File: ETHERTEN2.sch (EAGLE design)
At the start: 103 parts, among them IC1 MC33269DT-5.0, IC2 APX811-44UG-7, IC3 ATMEGA16U2-MU, IC4 LM358D, IC5 ATMEGA328P TQFP32, IC6 W5100SQFP80, IC7 MCP24AA025E48, J1 DC_2_1MM, P1 USB-6PSMT, P2 ICSP:MAIN, P3 ICSP:USB, P4 microSD, Q1 FDN340P, Q2 2N7002, Q3 2N7002, U1 HY931147C-RJ45, X1 16MHz, X2 25MHz, X3 16MHz

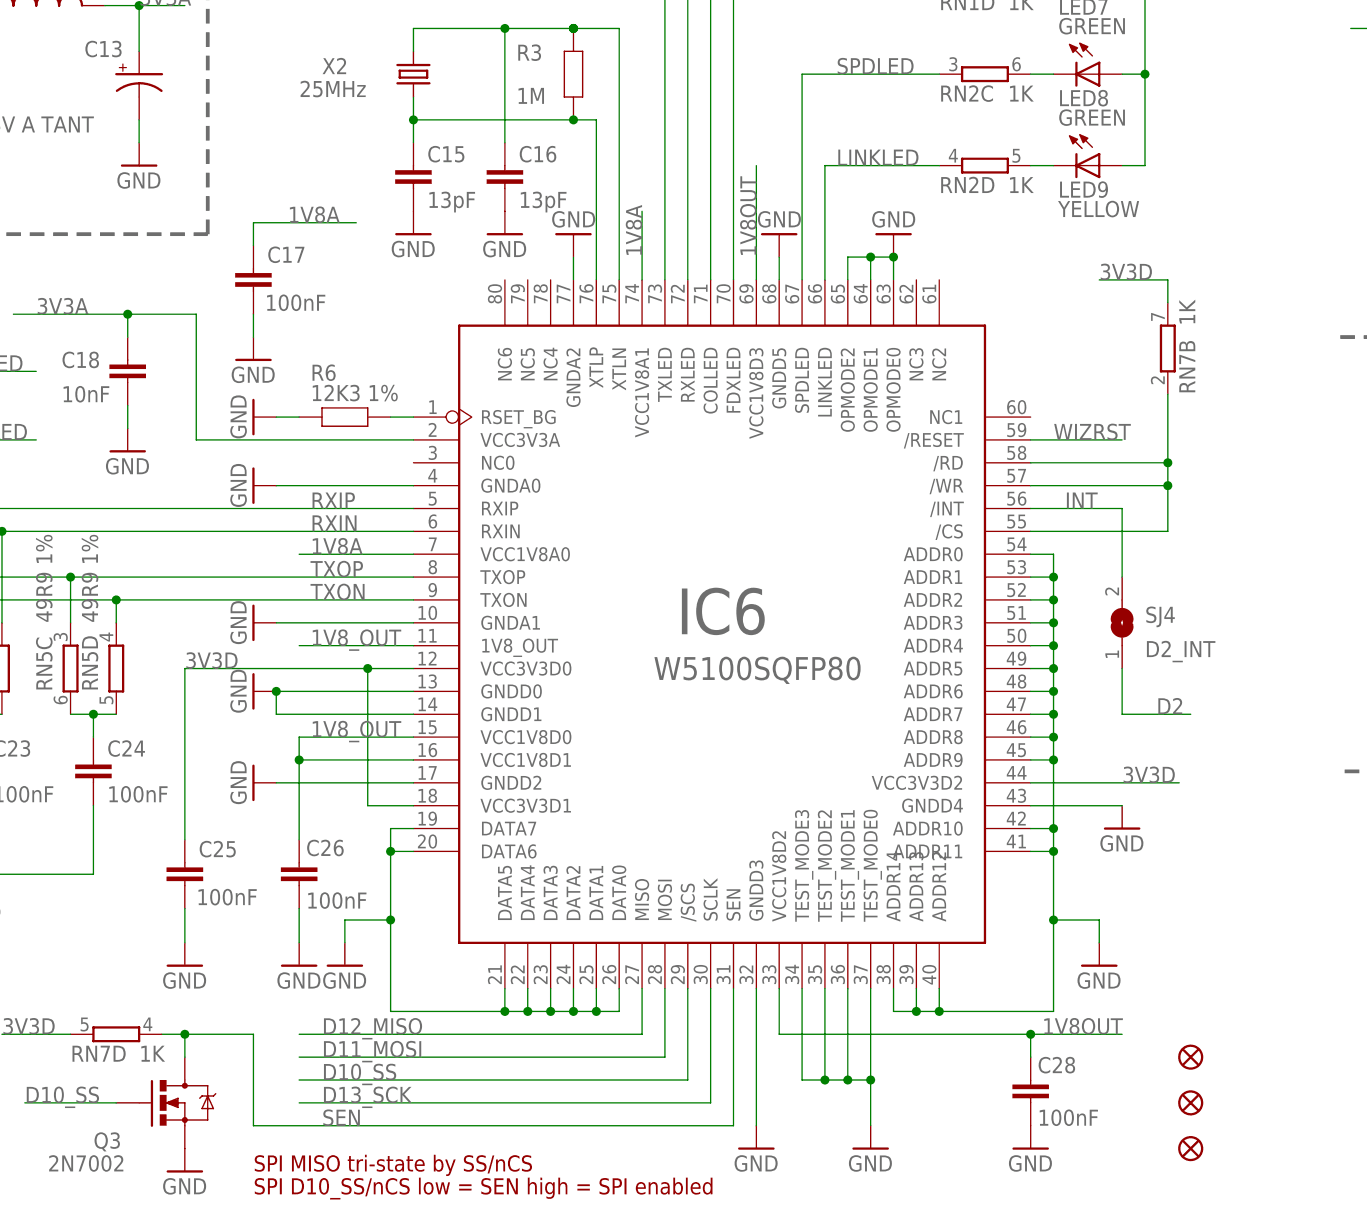
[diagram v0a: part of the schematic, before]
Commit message: Ethernet chip conversion
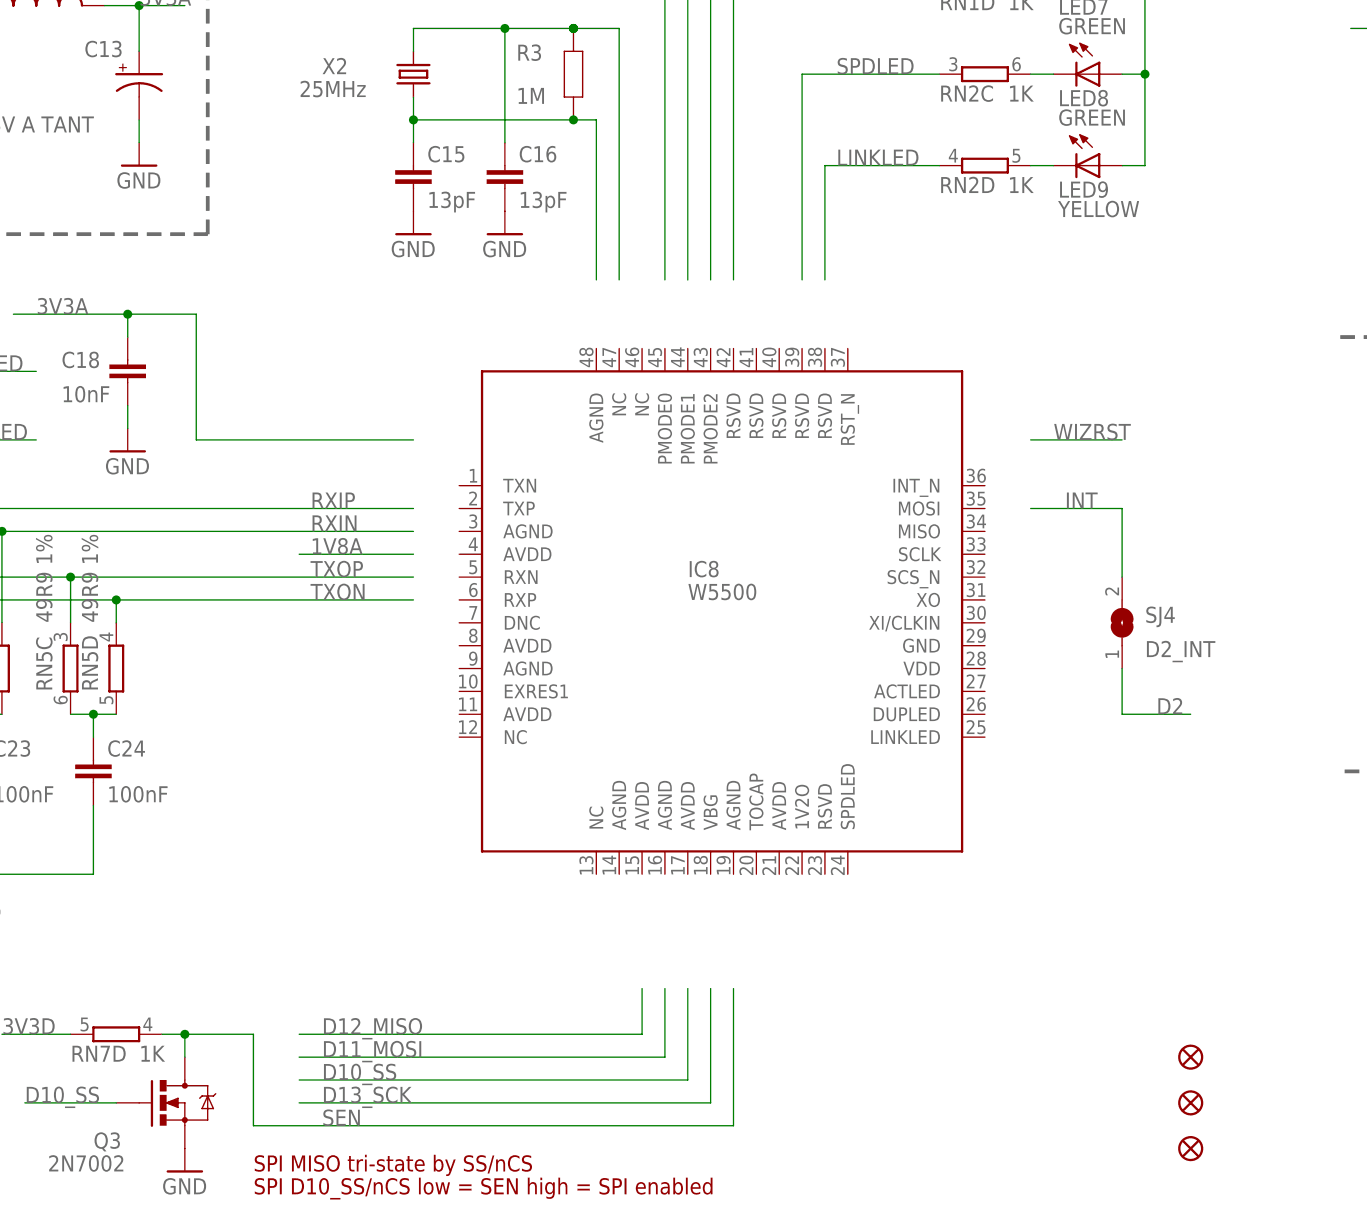
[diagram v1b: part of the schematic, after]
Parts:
- removed C17, C25, C26, C28: 100nF, freetronics:CAP0603
- removed IC6: W5100SQFP80, freetronics-marc:W5100SQFP80
- removed R6: 12K3 1%, freetronics:RESISTOR0603
- added IC8: W5500, W5500:W5500
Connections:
- removed net 1V8OUT: C28.1, IC6.VCC1V8D2, IC6.VCC1V8D3
- removed net N$27: IC6./CS, IC6./RD, IC6./WR, RN7B.1
- removed net N$322: IC6.RSET_BG, R6.2
- net 1V8A: no longer C17.1, IC6.VCC1V8A0, IC6.VCC1V8A1
- net 1V8_OUT: no longer C26.1, IC6.1V8_OUT, IC6.VCC1V8D0, IC6.VCC1V8D1
- net 3V3A: no longer IC6.VCC3V3A
- net 3V3D: no longer C25.1, IC6.VCC3V3D0, IC6.VCC3V3D1, IC6.VCC3V3D2, RN7B.2
- net COLLED: no longer IC6.COLLED
- net D10_SS: no longer IC6./SCS
- net D11_MOSI: no longer IC6.MOSI
- net D12_MISO: no longer IC6.MISO
- net D13_SCK: no longer IC6.SCLK
- net FDXLED: no longer IC6.FDXLED
- net GND: no longer C17.2, C25.2, C26.2, C28.2, IC6.ADDR0, IC6.ADDR1, IC6.ADDR10, IC6.ADDR11, IC6.ADDR12, IC6.ADDR13, IC6.ADDR14, IC6.ADDR2, IC6.ADDR3, IC6.ADDR4, IC6.ADDR5, IC6.ADDR6, IC6.ADDR7, IC6.ADDR8, IC6.ADDR9, IC6.DATA0, IC6.DATA1, IC6.DATA2, IC6.DATA3, IC6.DATA4, IC6.DATA5, IC6.DATA6, IC6.DATA7, IC6.GNDA0, IC6.GNDA1, IC6.GNDA2, IC6.GNDD0, IC6.GNDD1, IC6.GNDD2, IC6.GNDD3, IC6.GNDD4, IC6.GNDD5, IC6.OPMODE0, IC6.OPMODE1, IC6.OPMODE2, IC6.TEST_MODE0, IC6.TEST_MODE1, IC6.TEST_MODE2, IC6.TEST_MODE3, R6.1
- net INT: no longer IC6./INT
- net LINKLED: no longer IC6.LINKLED
- net RXIN: no longer IC6.RXIN
- net RXIP: no longer IC6.RXIP
- net SEN: no longer IC6.SEN
- net SPDLED: no longer IC6.SPDLED
- net TXON: no longer IC6.TXON
- net TXOP: no longer IC6.TXOP
- net WIZRST: no longer IC6./RESET
- net WRXLED: no longer IC6.RXLED
- net WTXLED: no longer IC6.TXLED
- net XTLN: no longer IC6.XTLN
- net XTLP: no longer IC6.XTLP
